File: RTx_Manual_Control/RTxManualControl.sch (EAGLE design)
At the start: 15 parts

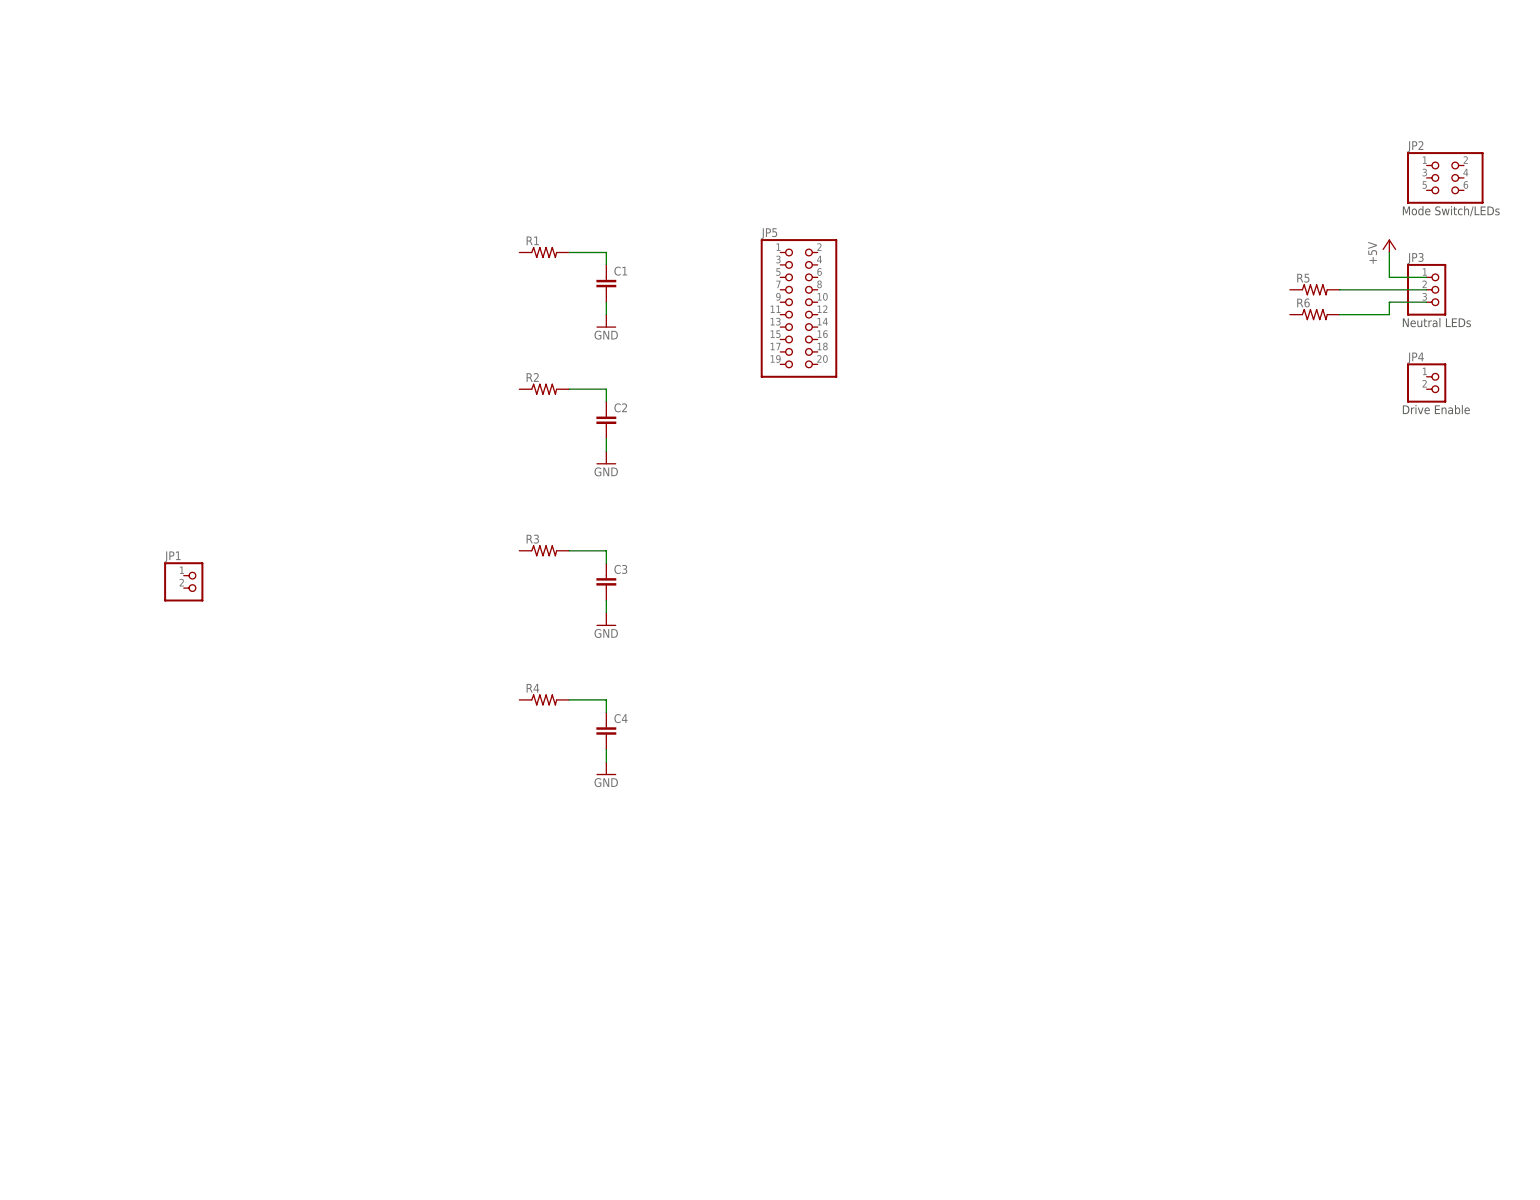
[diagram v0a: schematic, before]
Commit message: Completed draft of schematic without LPF component values. Need to determine LPF values, verify processor pinouts.
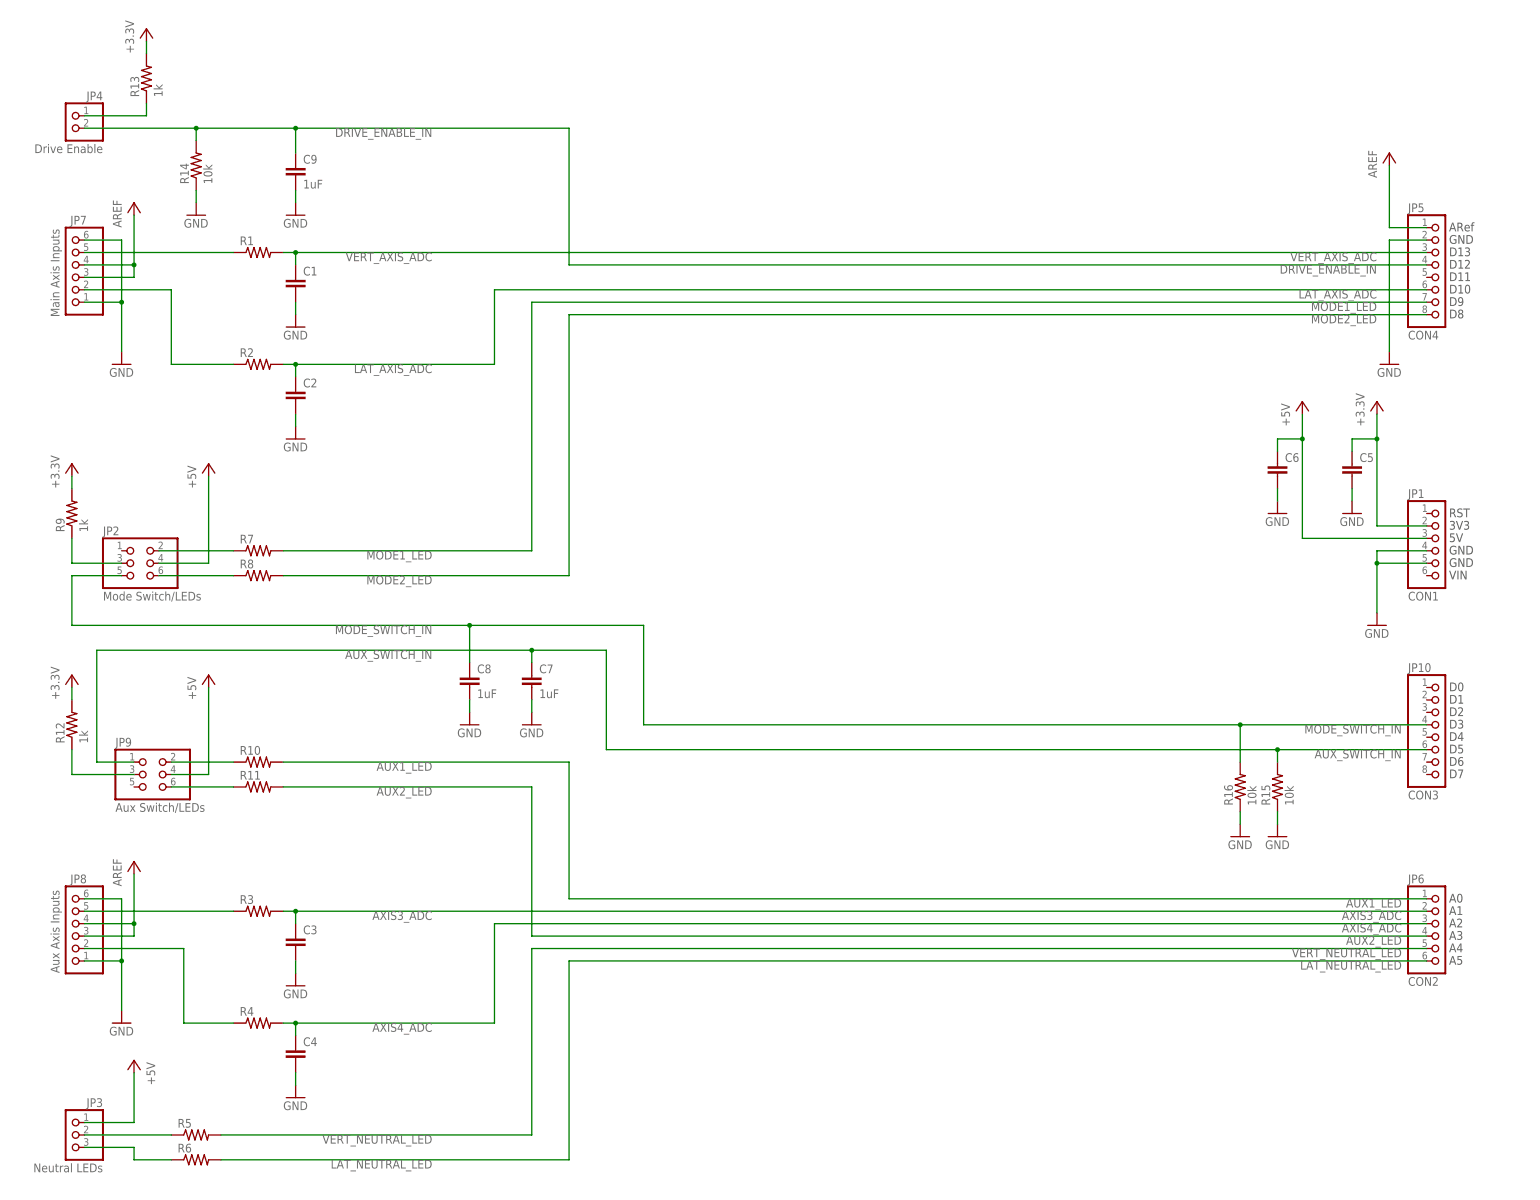
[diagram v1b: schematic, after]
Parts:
- added C5, C6: (no value), rcl:C-EUC1206
- added C7, C8, C9: 1uF, rcl:C-EUC1206
- added JP10: CON3, pinhead:PINHD-1X8
- added JP6: CON2, pinhead:PINHD-1X6
- added JP7: Main Axis Inputs, pinhead:PINHD-1X6
- added JP8: Aux Axis Inputs, pinhead:PINHD-1X6
- added JP9: Aux Switch/LEDs, pinhead:PINHD-2X3
- added R10, R11, R7, R8: (no value), rcl:R-US_R1206
- added R12, R13, R9: 1k, rcl:R-US_R1206
- added R14, R15, R16: 10k, rcl:R-US_R1206
- JP1: value (none) -> CON1; device pinhead:PINHD-1X2 -> pinhead:PINHD-1X6
- JP2: value (none) -> Mode Switch/LEDs
- JP3: value (none) -> Neutral LEDs
- JP4: value (none) -> Drive Enable
- JP5: value (none) -> CON4; device pinhead:PINHD-2X10 -> pinhead:PINHD-1X8
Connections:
- removed net CH1_ADC: C1.1, R1.2
- removed net CH2_ADC: C2.1, R2.2
- removed net CH3_ADC: C3.1, R3.2
- removed net CH4_ADC: C4.1, R4.2
- removed net N$1: JP3.3, R6.2
- removed net N$2: JP3.2, R5.2
- new net +3.3V: C5.1, JP1.2, R12.2, R13.2, R9.2
- new net AREF: JP5.1, JP7.3, JP7.4, JP8.3, JP8.4
- new net AUX1_LED: JP6.1, R10.2
- new net AUX1_LED_CONN: JP9.2, R10.1
- new net AUX2_LED: JP6.4, R11.2
- new net AUX2_LED_CONN: JP9.6, R11.1
- new net AUX_SWITCH_IN: C7.1, JP10.6, JP9.1, R15.2
- new net AUX_SWITCH_PULLUP: JP9.3, R12.1
- new net AXIS3_ADC: C3.1, JP6.2, R3.2
- new net AXIS3_CONN: JP8.5, R3.1
- new net AXIS4_ADC: C4.1, JP6.3, R4.2
- new net AXIS4_CONN: JP8.2, R4.1
- new net DRIVE_ENABLE_IN: C9.1, JP4.2, JP5.4, R14.2
- new net DRIVE_ENABLE_PULLUP: JP4.1, R13.1
- new net LAT_AXIS_ADC: C2.1, JP5.6, R2.2
- new net LAT_AXIS_CONN: JP7.2, R2.1
- new net LAT_NEAUTRAL_LED_CONN: JP3.3, R6.1
- new net LAT_NEUTRAL_LED: JP6.6, R6.2
- new net MODE1_LED: JP5.7, R7.2
- new net MODE1_LED_CONN: JP2.2, R7.1
- new net MODE2_LED: JP5.8, R8.2
- new net MODE2_LED_CONN: JP2.6, R8.1
- new net MODE_SWITCH_IN: C8.1, JP10.4, JP2.5, R16.2
- new net MODE_SWITCH_PULLUP: JP2.3, R9.1
- new net VERT_AXIS_ADC: C1.1, JP5.3, R1.2
- new net VERT_AXIS_CONN: JP7.5, R1.1
- new net VERT_NEUTRAL_LED: JP6.5, R5.2
- new net VERT_NEUTRAL_LED_CONN: JP3.2, R5.1
- net +5V: now also C6.1, JP1.3, JP2.4, JP9.4
- net GND: now also C5.2, C6.2, C7.2, C8.2, C9.2, JP1.4, JP1.5, JP5.2, JP7.1, JP7.6, JP8.1, JP8.6, R14.1, R15.1, R16.1
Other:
- note added: "3V3"
- note added: "5V"
- note added: "A0"
- note added: "A1"
- note added: "A2"
- note added: "A3"
- note added: "A4"
- note added: "A5"
- note added: "ARef"
- note added: "D0"
- note added: "D1"
- note added: "D10"
- note added: "D11"
- note added: "D12"
- note added: "D13"
- note added: "D2"
- note added: "D3"
- note added: "D4"
- note added: "D5"
- note added: "D6"
- note added: "D7"
- note added: "D8"
- note added: "D9"
- note added: "GND"
- note added: "RST"
- note added: "VIN"
- note removed: "Drive Enable"
- note removed: "Mode Switch/LEDs"
- note removed: "Neutral LEDs"
- moved on the sheet: C1, C2, C3, C4, JP2, JP3, JP4, R1, R2, R3, R4, R5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

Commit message: Changed pinout of Neutral LED connector. Added supply rail decoupling cap values, ARef decoupling cap.
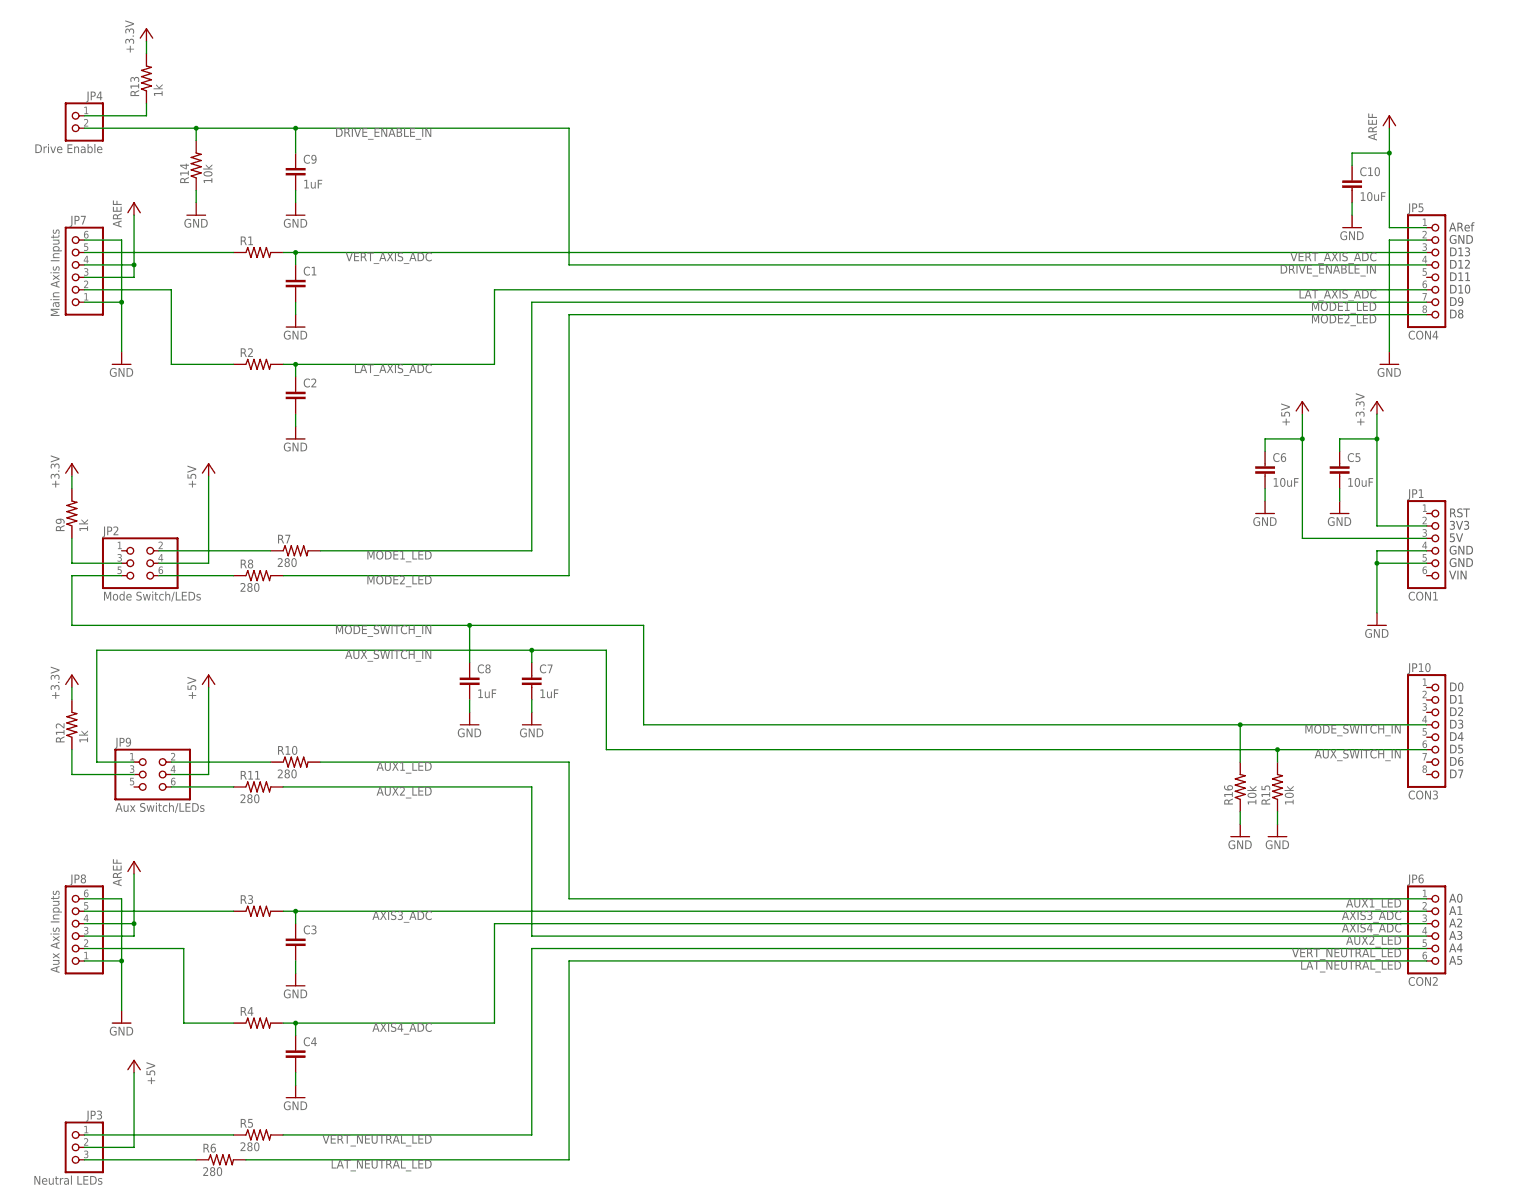
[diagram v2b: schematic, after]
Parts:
- added C10: 10uF, rcl:C-EUC1206
- C5, C6: value (none) -> 10uF
- R10, R11, R5, R6, R7, R8: value (none) -> 280
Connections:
- net +5V: now also JP3.2; no longer JP3.1
- net AREF: now also C10.1
- net GND: now also C10.2
- net VERT_NEUTRAL_LED_CONN: now also JP3.1; no longer JP3.2
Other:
- moved on the sheet: C5, C6, JP3, R10, R5, R6, R7

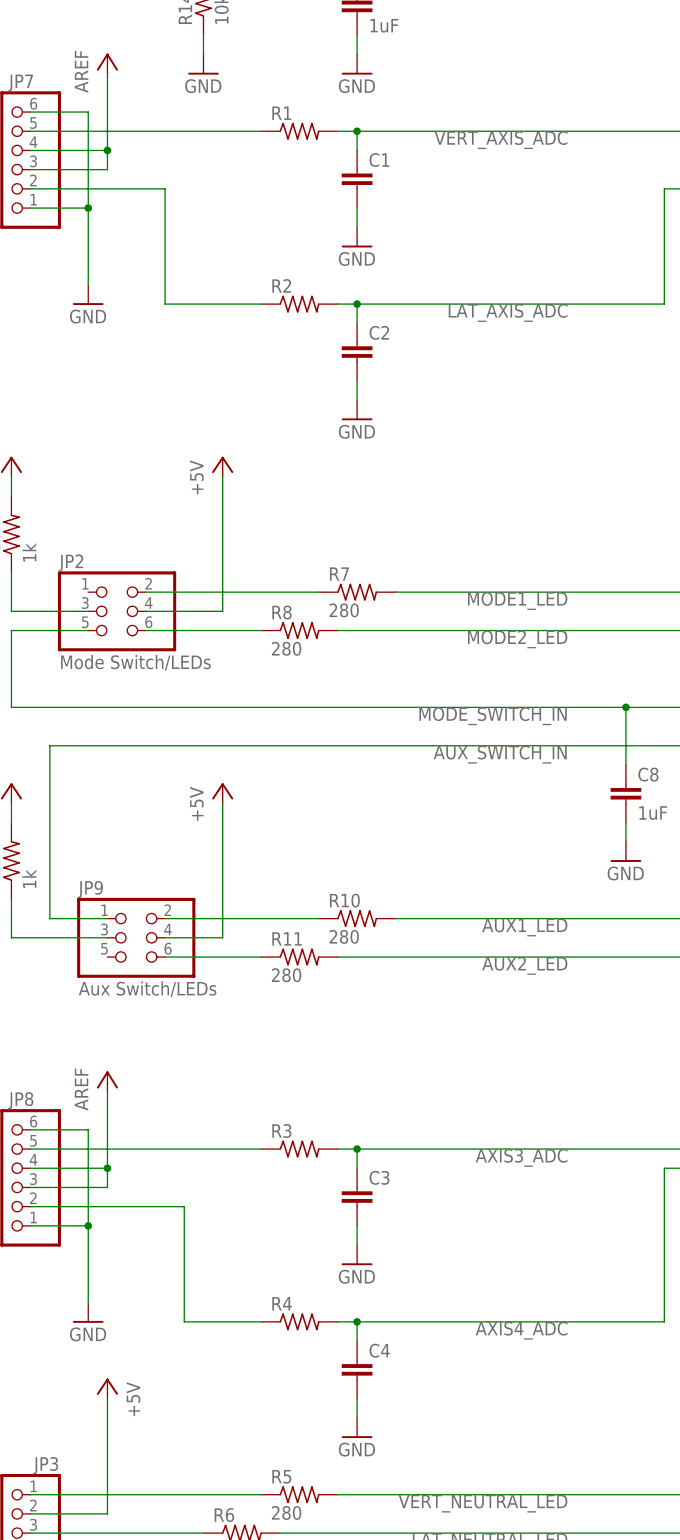
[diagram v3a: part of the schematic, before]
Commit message: Added values for manual input LPF components. Completed RTx Manual Remote Design document.
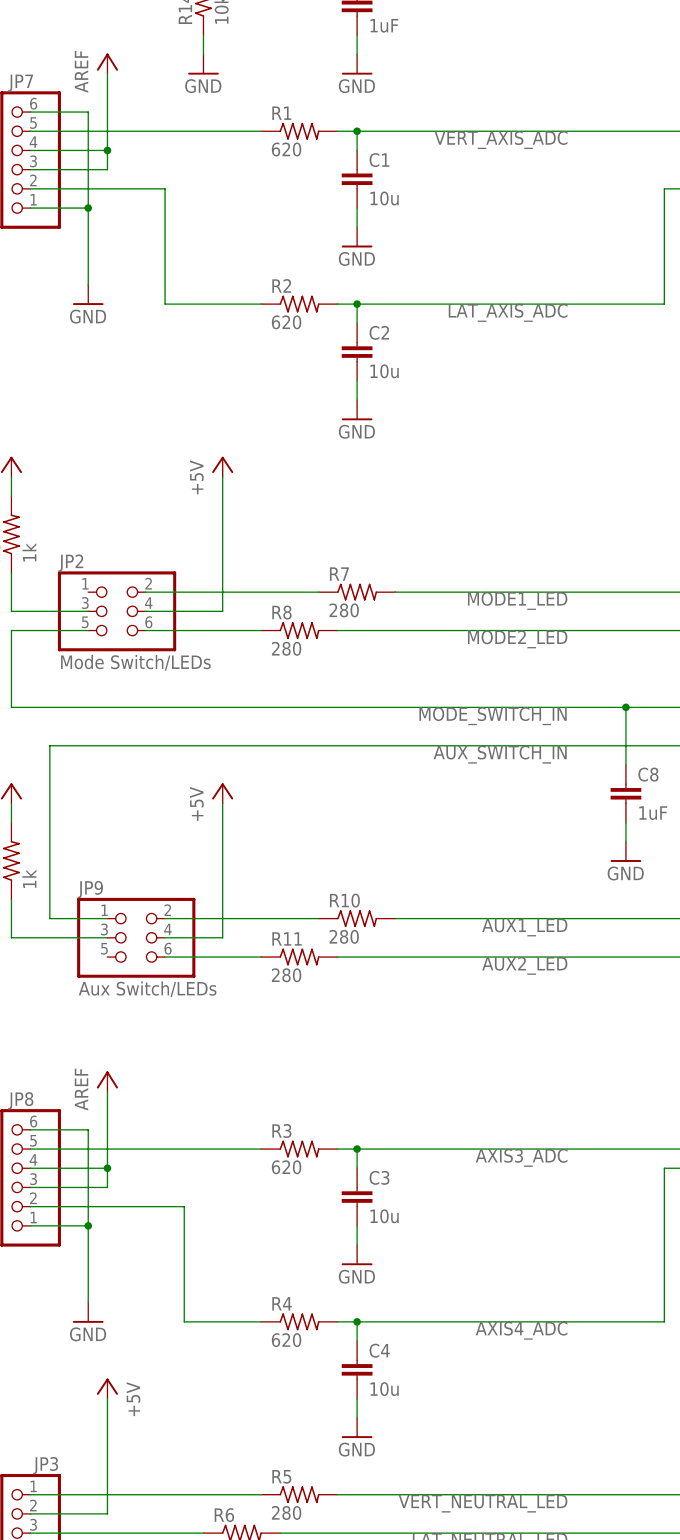
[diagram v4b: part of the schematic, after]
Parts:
- C1, C2, C3, C4: value (none) -> 10u
- R1, R2, R3, R4: value (none) -> 620
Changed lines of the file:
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@@
 <parts>
 <part name="U$1" library="motorFeedback" deviceset="FRAME" device=""/>
-<part name="C1" library="rcl" deviceset="C-EU" device="C1206"/>
-<part name="C2" library="rcl" deviceset="C-EU" device="C1206"/>
-<part name="C3" library="rcl" deviceset="C-EU" device="C1206"/>
-<part name="C4" library="rcl" deviceset="C-EU" device="C1206"/>
-<part name="R1" library="rcl" deviceset="R-US_" device="R1206"/>
-<part name="R2" library="rcl" deviceset="R-US_" device="R1206"/>
-<part name="R3" library="rcl" deviceset="R-US_" device="R1206"/>
-<part name="R4" library="rcl" deviceset="R-US_" device="R1206"/>
+<part name="C1" library="rcl" deviceset="C-EU" device="C1206" value="10u"/>
+<part name="C2" library="rcl" deviceset="C-EU" device="C1206" value="10u"/>
+<part name="C3" library="rcl" deviceset="C-EU" device="C1206" value="10u"/>
+<part name="C4" library="rcl" deviceset="C-EU" device="C1206" value="10u"/>
+<part name="R1" library="rcl" deviceset="R-US_" device="R1206" value="620"/>
+<part name="R2" library="rcl" deviceset="R-US_" device="R1206" value="620"/>
+<part name="R3" library="rcl" deviceset="R-US_" device="R1206" value="620"/>
+<part name="R4" library="rcl" deviceset="R-US_" device="R1206" value="620"/>
 <part name="GND1" library="supply1" deviceset="GND" device=""/>
 <part name="GND2" library="supply1" deviceset="GND" device=""/>
